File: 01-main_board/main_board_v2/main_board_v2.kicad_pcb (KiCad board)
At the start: 4 copper layers, 96.4 x 65.3 mm, 158 parts, among them IC1 MAX6105EUR+T, IC10 ESP32-S3, IC11 LT3973EMSE-5#PBF, IC2 LP5907MFX-2.5_NOPB, IC3 TS3USB30EDGSR, IC4 SPX3819S-L_TR, IC5 INA827AIDGK, IC6 AD7175-8BCPZ-RL7, IC7 INA827AIDGK, IC8 AD8591ARTZ-REEL7, IC9 LSF0108PWR, J1 Mezzanine Edge, J4 DB44 (Analog | Digital), T1 749013011, U1 Teensy4.1, U2 AD5689RARUZ-RL7, U3 MCP2562FD-E/SN, U4 TPS2115APWR, Y1 ECS-400-10-37B2-CKY-TR, Y2 ECS-.327-12.5-34B-TR

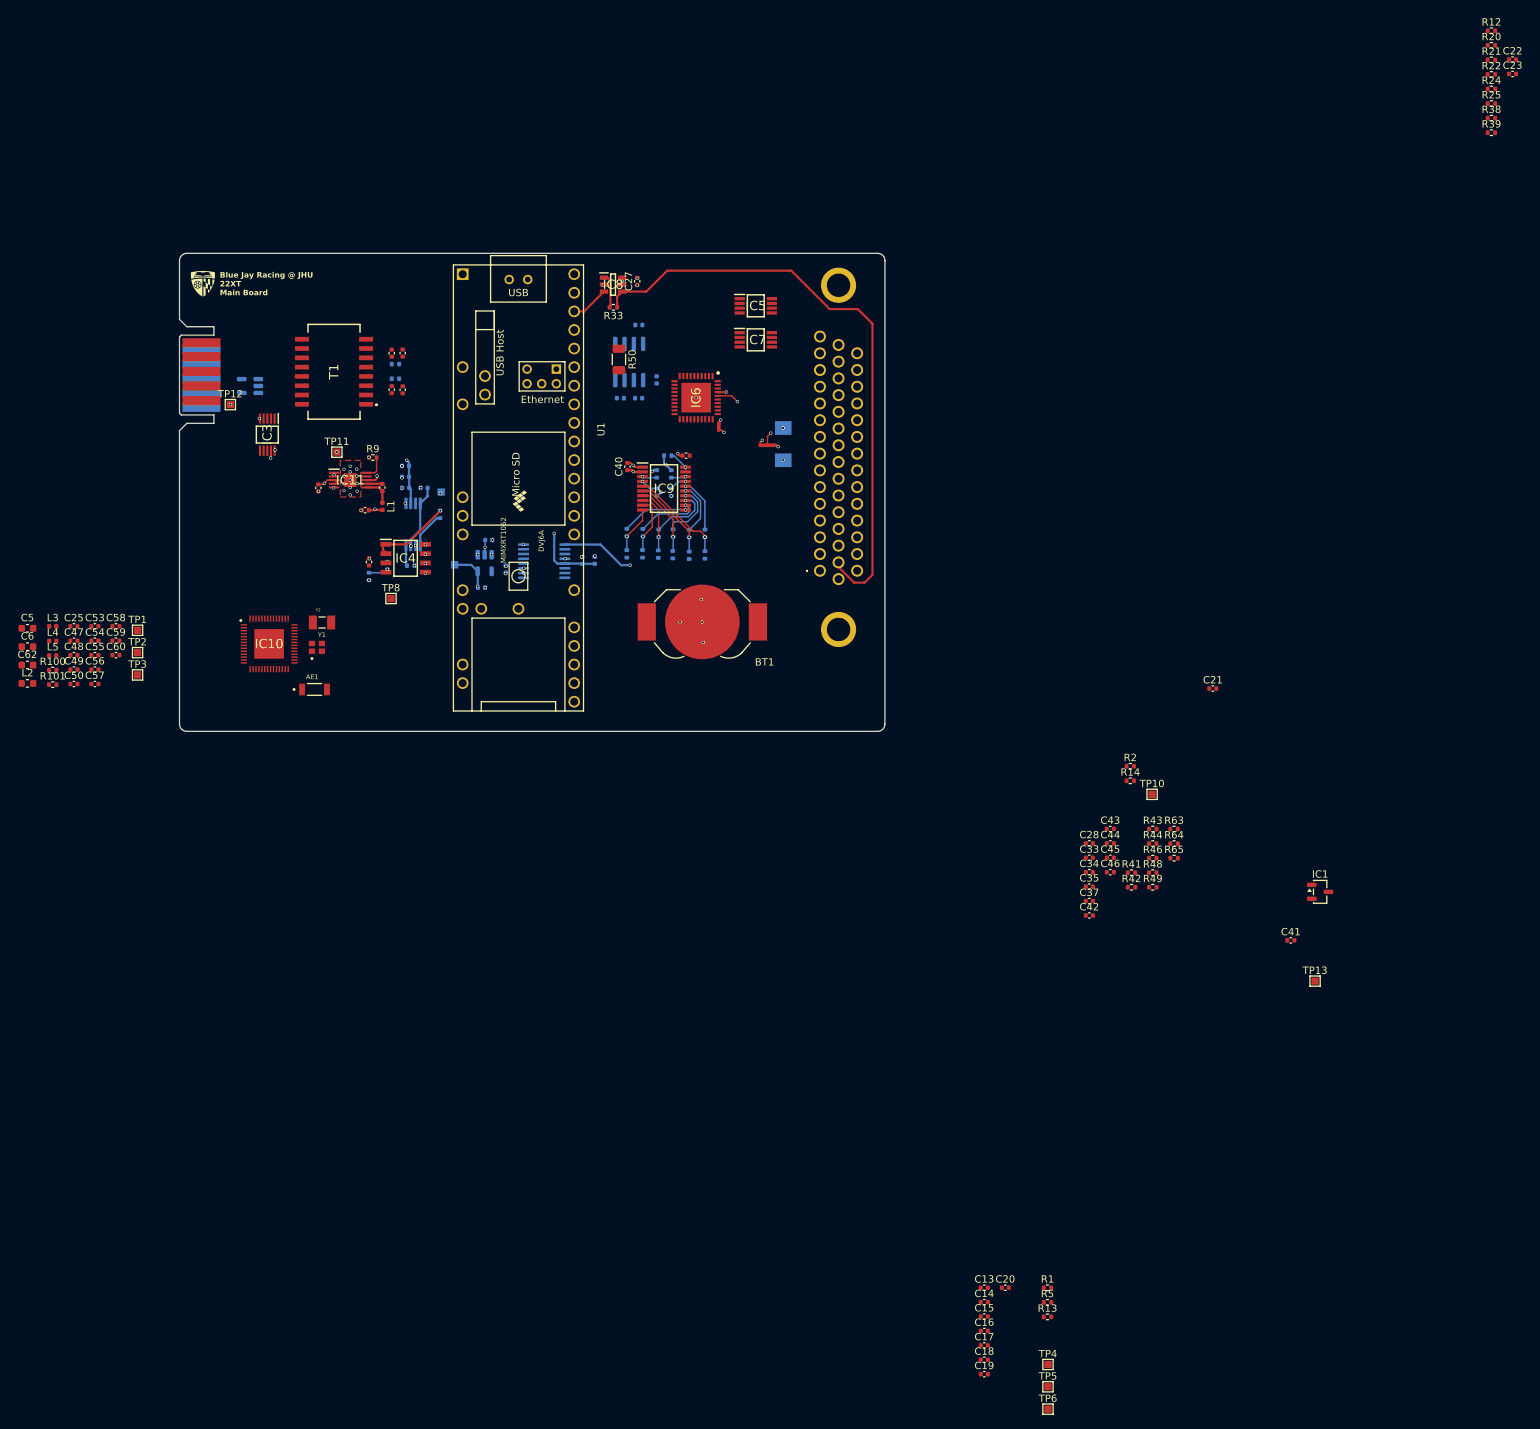
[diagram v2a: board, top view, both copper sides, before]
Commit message: finished sensor input layout and some spi bus
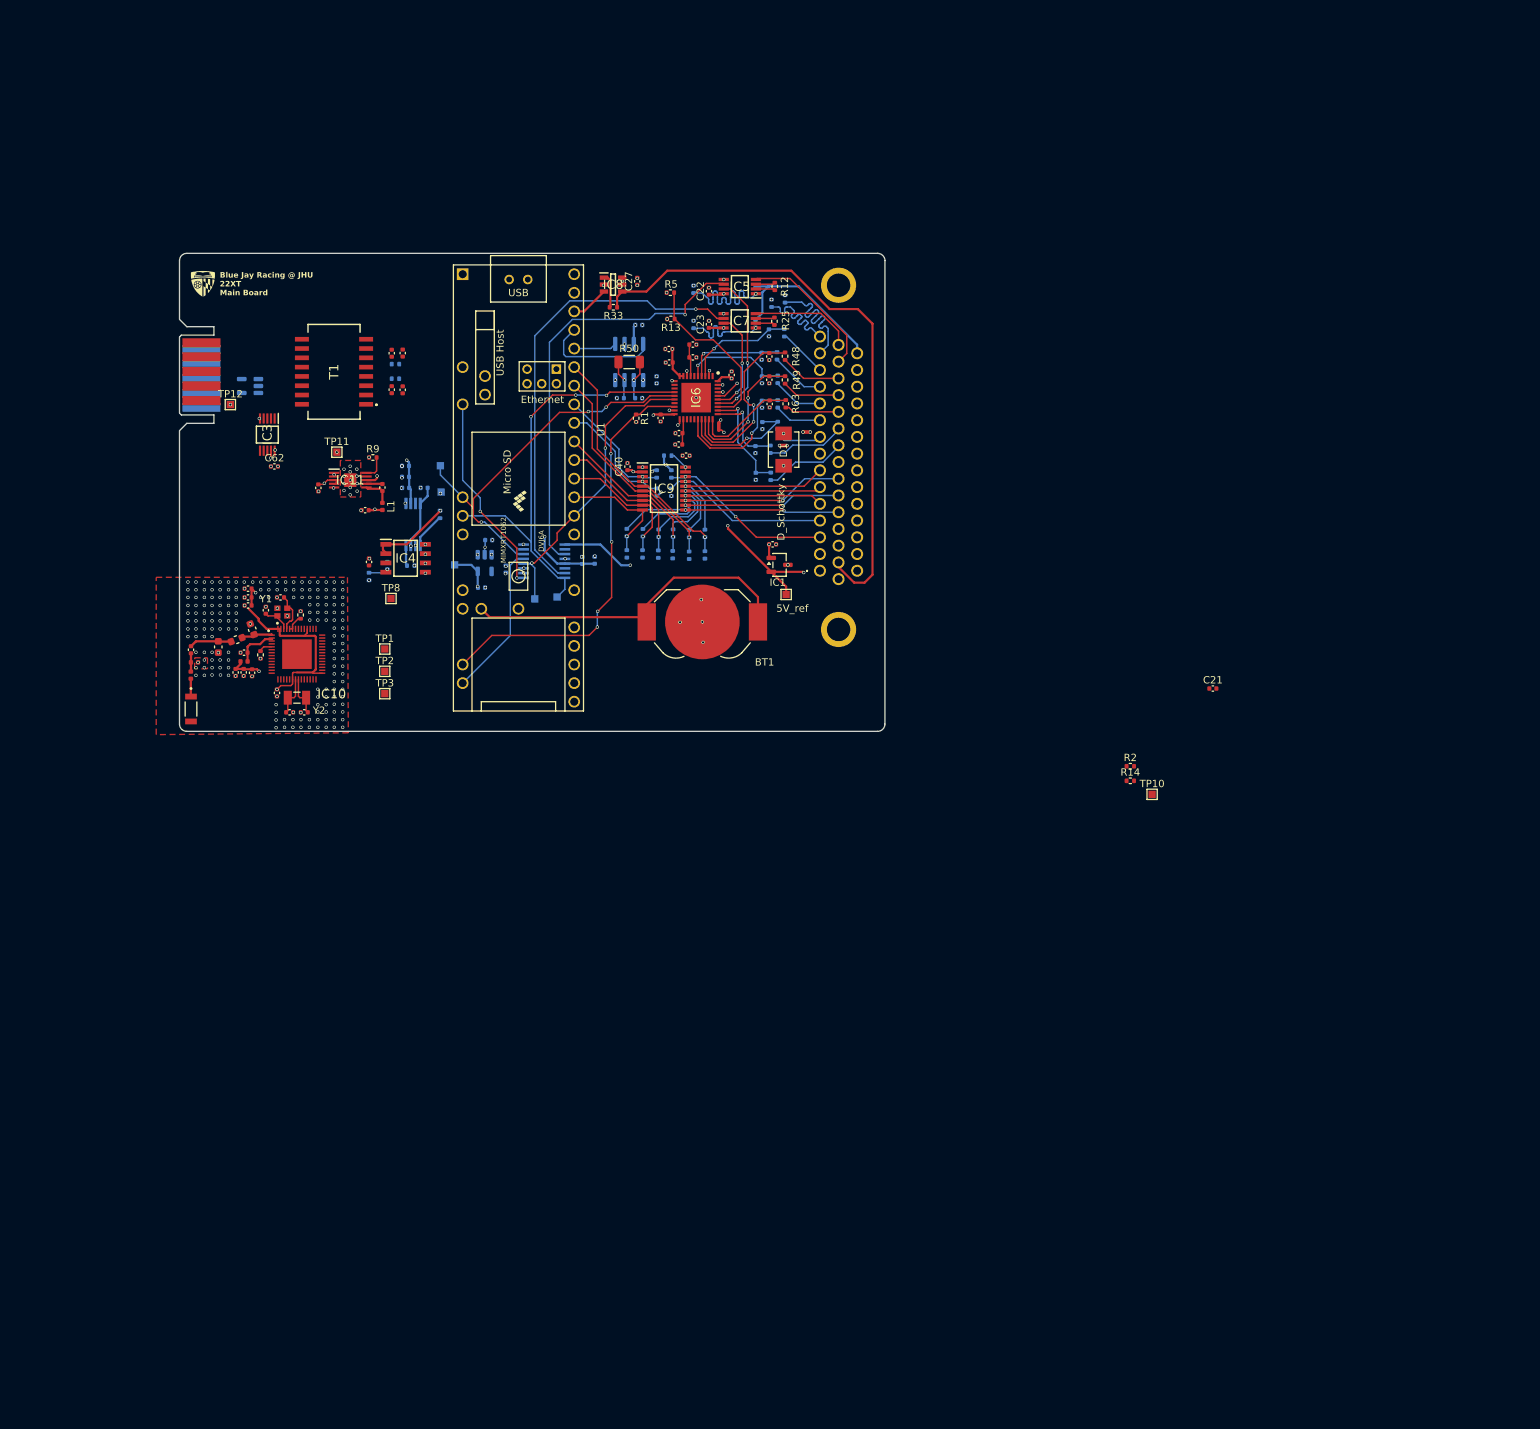
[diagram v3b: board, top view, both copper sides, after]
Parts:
- added NT3: NetTie_2, NetTie:NetTie-2_SMD_Pad0.5mm, F.Cu at (127.2, 45.1)
- C28, C33, C34, C35, C37, C45, C46, R20, R21, R22, R24, R38, R39, R41, R42, R43, R44, R46, R64, R65, TP4, TP5, TP6: moved to B.Cu
- C62: footprint Capacitor_SMD:C_0603_1608Metric -> Capacitor_SMD:C_0402_1005Metric
- D1: moved to F.Cu
- NT2: value NetTie_3_Tee -> NetTie_2; footprint NetTie:NetTie-3_SMD_Pad0.5mm -> NetTie:NetTie-2_SMD_Pad0.5mm
- moved TP5 150.8 mm to (77.2, 49.7), turned to 180 degrees
- moved R5 147.3 mm to (108.6, 26.1)
- moved R13 145.8 mm to (108.7, 29.6), turned to 180 degrees
- moved C18 144.3 mm to (111.7, 33.1)
- moved C16 139.2 mm to (108.4, 35.6), turned to 180 degrees
- moved C15 139.1 mm to (108.4, 33.8), turned to 180 degrees
- moved C17 137.0 mm to (117.0, 37.3), turned to -90 degrees
- moved C19 135.2 mm to (109.8, 45.2), turned to 180 degrees
- moved C13 133.2 mm to (111.7, 34.9)
- moved R1 131.5 mm to (103.9, 43.2), turned to -90 degrees
- moved TP6 131.1 mm to (90.0, 67.9)
- moved C20 127.8 mm to (107.2, 43.2), turned to -90 degrees
- moved TP4 124.5 mm to (93.1, 67.7), turned to 180 degrees
- moved C14 124.4 mm to (109.7, 46.8), turned to 180 degrees
- moved C23 115.0 mm to (113.8, 30.4), turned to 90 degrees
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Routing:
- net 5V_ref: track 0.00 -> 65.0 mm, vias 0 -> 3
- net bias_B: track 0.00 -> 63.5 mm, vias 0 -> 1
- net MISO1: track 0.00 -> 59.7 mm, vias 0 -> 3
- net bias_A: track 0.00 -> 58.4 mm, vias 0 -> 1
- net !ERROR: track 0.00 -> 57.8 mm, vias 0 -> 4
- net MOSI1: track 0.00 -> 52.7 mm, vias 0 -> 3
- net Net-(BT1-+): track 0.00 -> 48.2 mm
- net SCLK1: track 0.00 -> 41.2 mm, vias 0 -> 2
- net 3V3: track 0.00 -> 33.3 mm, vias 0 -> 3
- net !LDAC: track 0.00 -> 27.7 mm, vias 0 -> 2
- net A6_nyq: track 0.00 -> 24.7 mm, vias 0 -> 2
- net 2V5: track 8.79 -> 32.9 mm
- net Net-(IC6-AIN11): track 0.00 -> 23.4 mm
- net DN4: track 8.39 -> 30.5 mm, vias 1 -> 2
- net SCL_mag: track 2.14 -> 24.1 mm, vias 1 -> 2
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- added copper zone on F.Cu, net GNDD

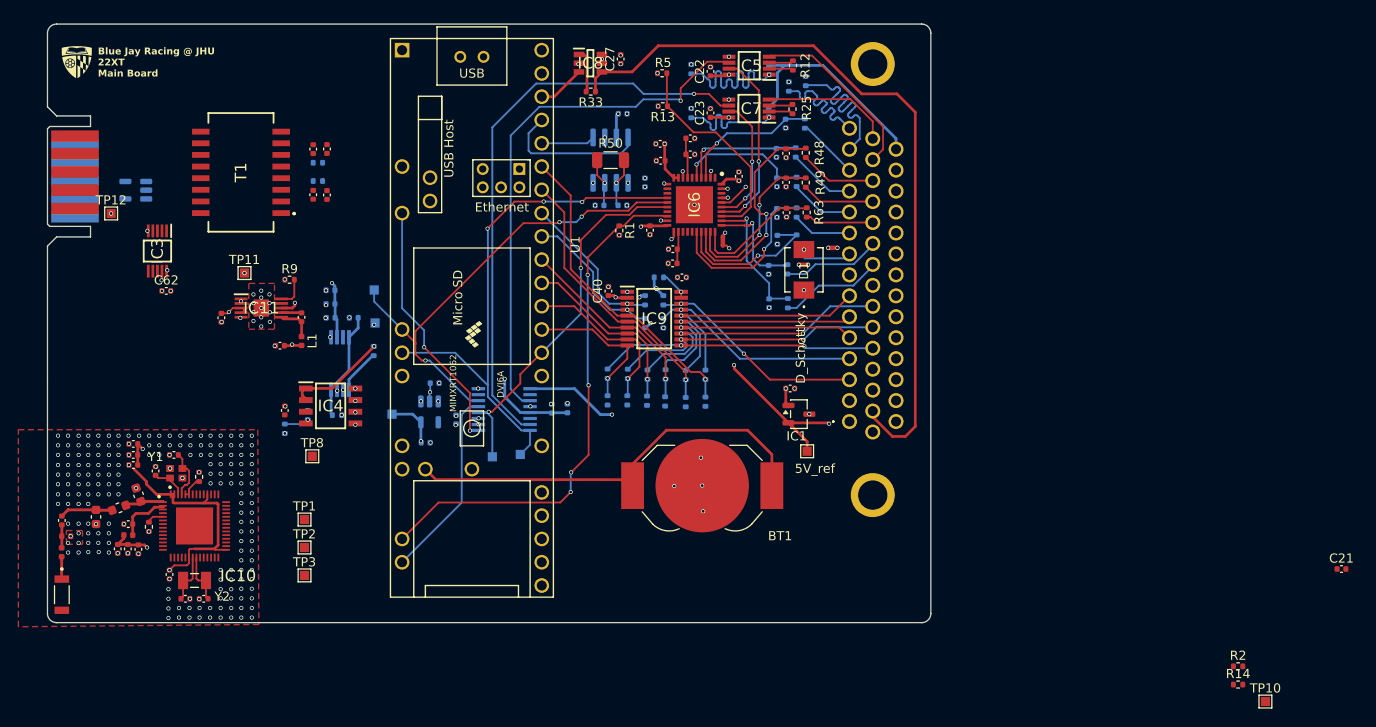
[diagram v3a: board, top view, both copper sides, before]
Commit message: condensed board size, routed ethernet, finalized non esp32 and non mezzanine related connections
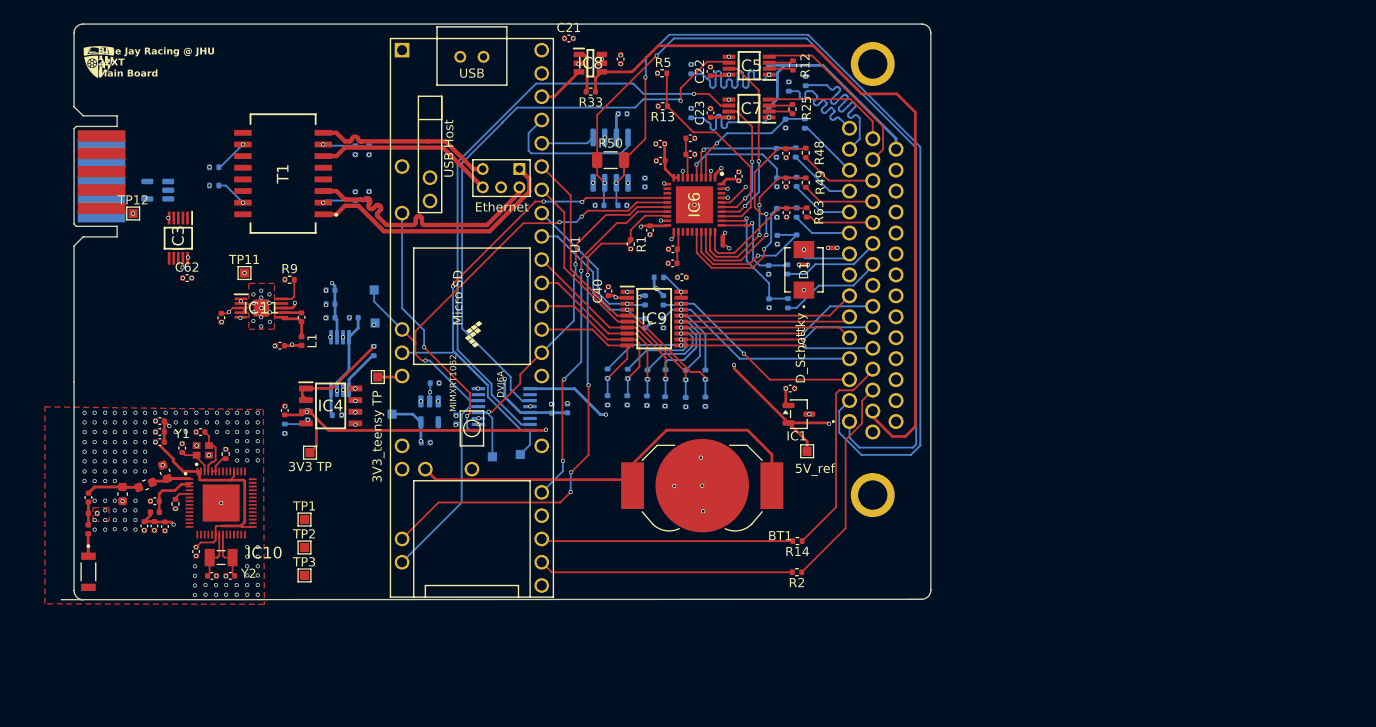
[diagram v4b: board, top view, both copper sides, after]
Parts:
- C29, C30, C31, C32: moved to B.Cu
- moved TP10 103.1 mm to (77.5, 59.2)
- moved C21 102.3 mm to (98.4, 22.2)
- moved R14 50.6 mm to (123.3, 77.1), turned to 180 degrees
- moved R2 49.2 mm to (123.3, 80.5), turned to 180 degrees
- moved R27 11.6 mm to (59.7, 38.3), turned to 0 degrees
- moved R28 11.4 mm to (59.7, 36.3), turned to 0 degrees
- moved C29 6.10 mm to (76.6, 34.5)
- moved C31 6.10 mm to (76.6, 39.4)
- moved T1 4.60 mm to (67.2, 37.0)
- moved C47 3.83 mm to (56.2, 67.0)
- moved C48 3.83 mm to (58.2, 65.2)
- moved C49 3.83 mm to (59.5, 80.9)
- moved C50 3.83 mm to (61.5, 80.9)
- moved C57 3.83 mm to (53.8, 66.3)
- moved C58 3.83 mm to (53.8, 65.2)
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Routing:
- net CANL: track 5.36 -> 100.6 mm, vias 1 -> 2
- net CANH: track 5.32 -> 95.5 mm, vias 1 -> 2
- net 3V3: track 33.3 -> 109.1 mm, vias 3 -> 6
- net !CS_ADC: track 0.00 -> 38.9 mm, vias 0 -> 3
- net RD+: track 0.00 -> 28.7 mm
- net RD-: track 0.00 -> 28.6 mm
- net Net-(U1-34_RX8): track 0.00 -> 27.8 mm
- net Net-(U1-35_TX8): track 0.00 -> 27.5 mm
- net GP/Int2: track 0.00 -> 23.1 mm
- net GP/Int1: track 0.00 -> 22.9 mm
- net TD+: track 0.00 -> 19.6 mm
- net TD-: track 0.00 -> 19.6 mm
- net bias_A: track 58.4 -> 64.3 mm
- net Net-(T1-TCT): track 0.00 -> 5.29 mm, vias 0 -> 1
- net Net-(T1-RCT): track 0.00 -> 5.10 mm, vias 0 -> 1
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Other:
- board size 96.4 x 65.3 mm -> 94.9 x 62.8 mm
